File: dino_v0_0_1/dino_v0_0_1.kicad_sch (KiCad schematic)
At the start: 17 parts, among them SW1 SW_DIP_x07, U1 74LS590, U2 74LS590, U3 NE555P

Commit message: Schematic WIP
Updated Document as well.
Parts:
- added B1: Reset, symbol Switch:SW_Push
- added C1: 1µF, symbol Device:C_Small
- added C2: 0.1µF, symbol Device:C_Small
- added R1: R, symbol Device:R
- added R1: 1kΩ, symbol Device:R
- added R2: 100kΩ, symbol Device:R
- B2: renamed from Write; value Button 1 -> Write
- B3: renamed from Increment; value Button 2 -> Increment Addr
- MCM60256AP: value ~ -> SRAM
- SPDT: renamed from RUN/LOAD; value Mode Switch -> LOAD/RUN
- renumbered 74LS1 to 74LS645, U2 to HighCounter, U1 to LowCounter, U3 to SystemTimer
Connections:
- net ASTABLE_MODE: now reaches SystemTimer.2 (TR)
- net ASTABLE_MODE: now also SystemTimer.6 (THR), C1.1, R2.2
- net Timer output: now reaches SystemTimer.3 (Q)
- net Timer output: now also LowCounter.11 (CPC)
- net at SystemTimer.5 (CV): now also C2.1
- net at SystemTimer.7 (DIS): now also R1.2, R2.1
- net RESET: now reaches LowCounter.10 (~{MRC})
- net RESET: now also HighCounter.10 (~{MRC}), B1.1
- net Ripple Cascade: now reaches LowCounter.9 (~{RCO})
- net Ripple Cascade: now also HighCounter.11 (CPC)
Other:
- moved on the sheet: 74LS645, D1, D2, D3, D4, D5, D6, D7, D8, HighCounter, LowCounter, MCM60256AP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

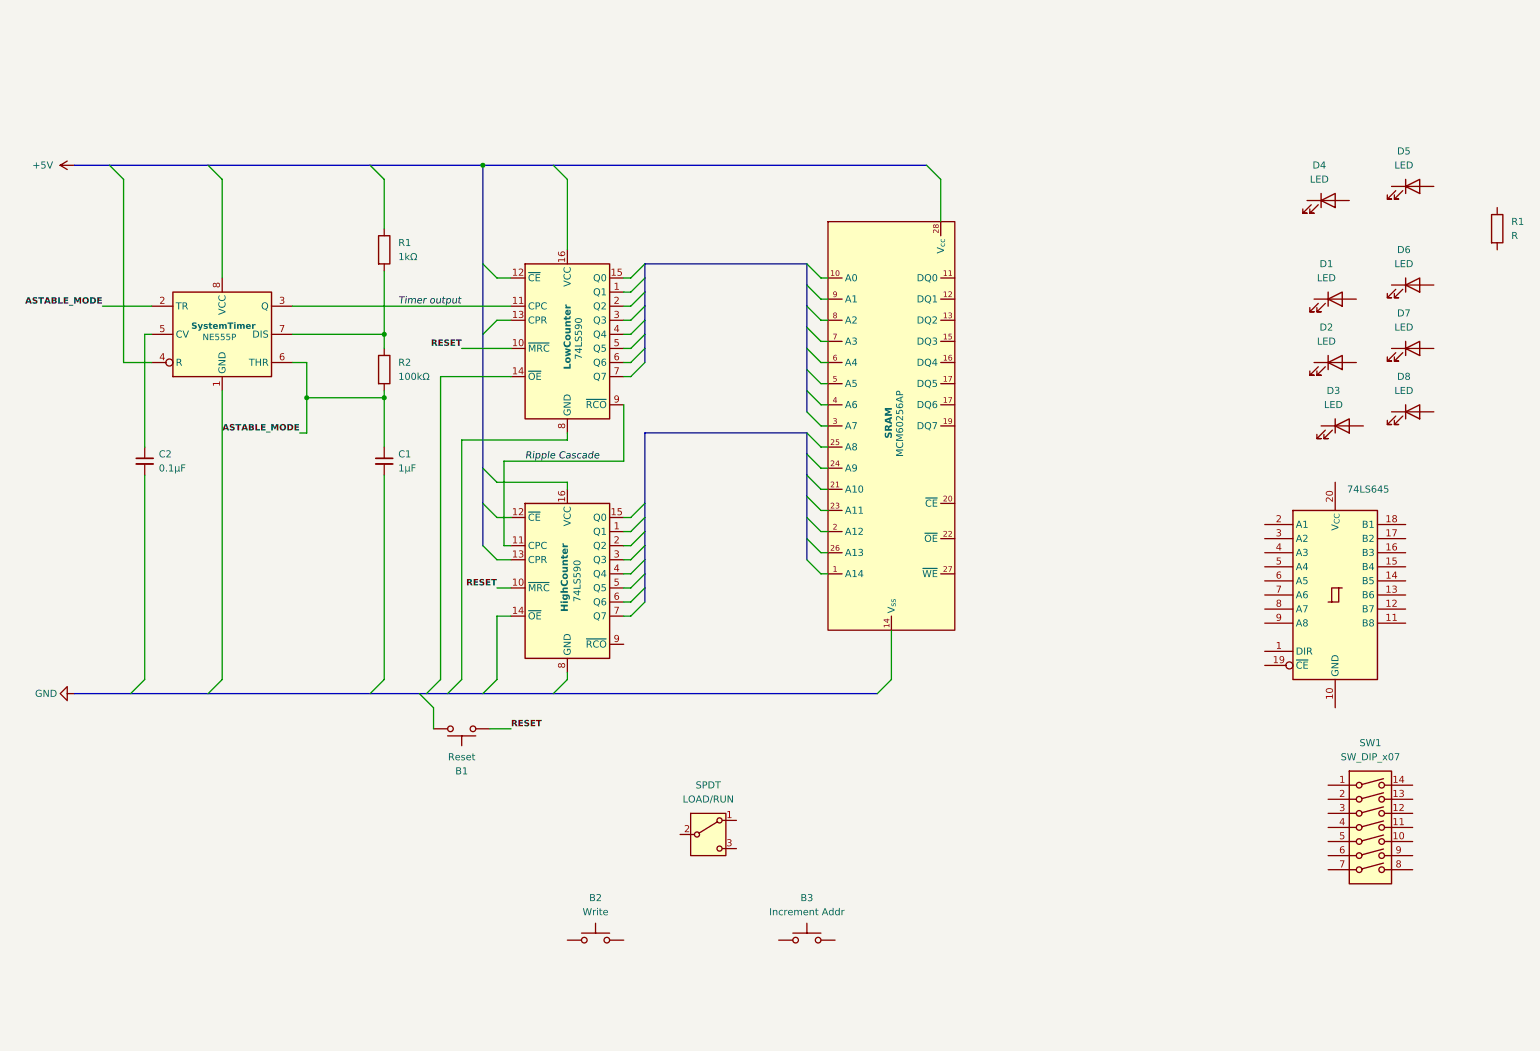
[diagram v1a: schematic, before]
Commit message: Updated D.I.N.O v0.0.2 Schematic
Discrete Integrated NISC Operator
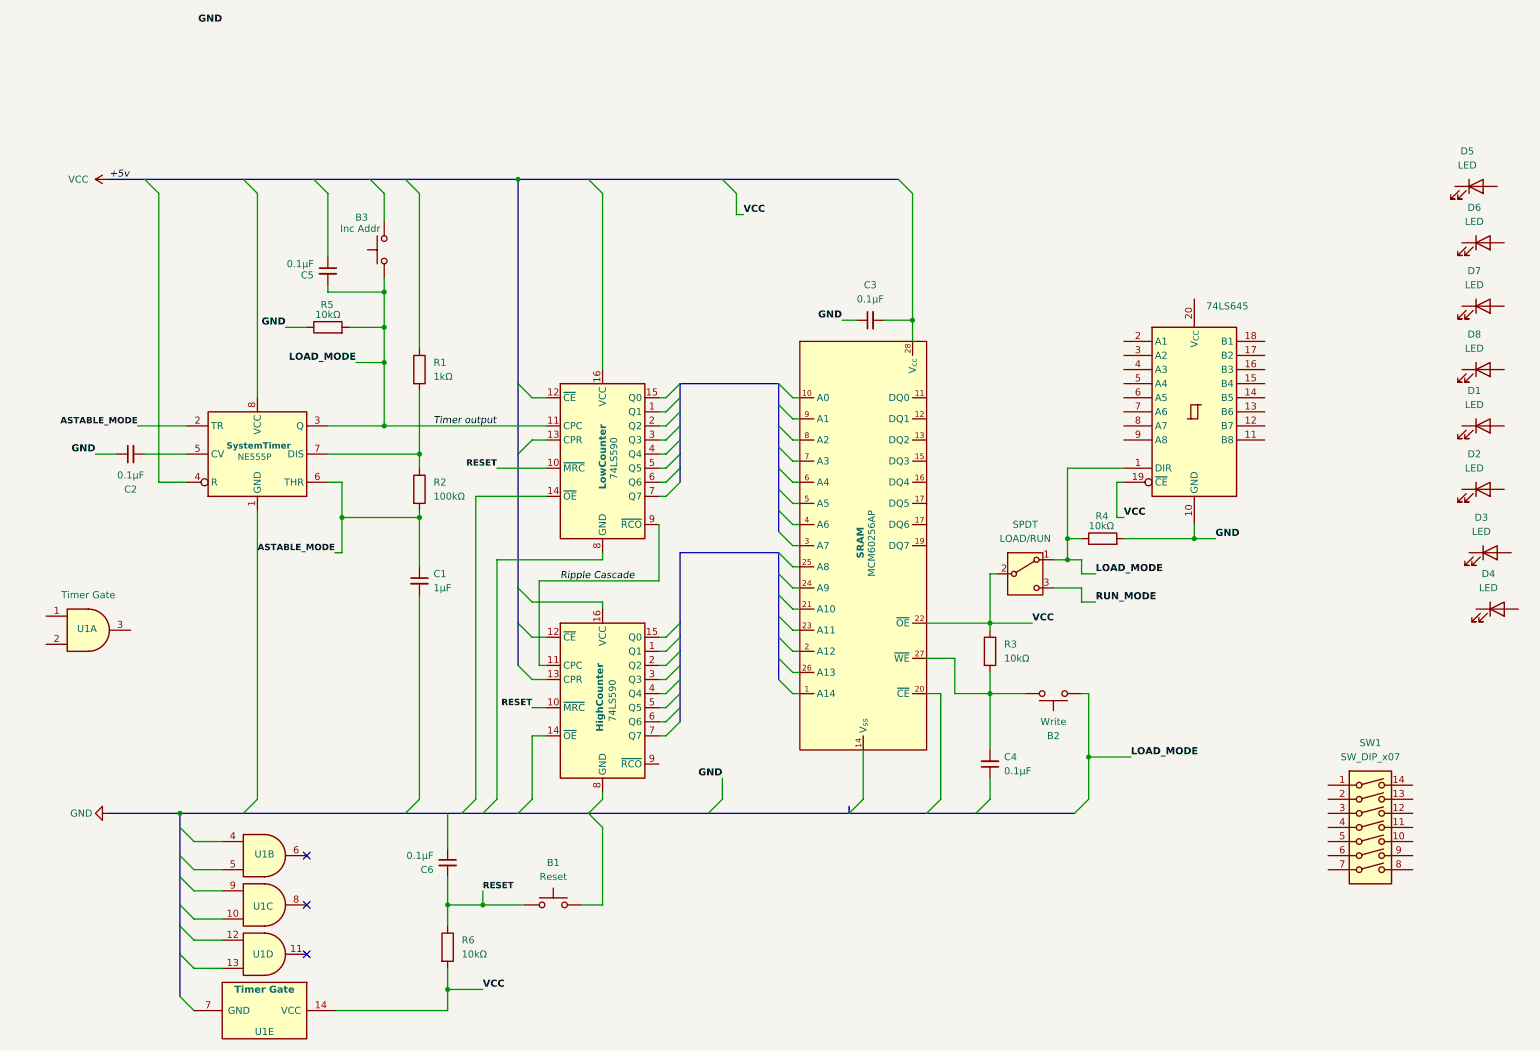
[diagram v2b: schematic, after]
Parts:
- removed R1: R, symbol Device:R
- added C3, C4, C5, C6: 0.1µF, symbol Device:C_Small
- added R3, R4, R5, R6: 10kΩ, symbol Device:R
- added U1: Timer Gate, symbol 74xx:74LS08
- B3: value Increment Addr -> Inc Addr
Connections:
- net Timer output is gone; now on net LOAD_MODE: LowCounter.11 (CPC), SystemTimer.3 (Q)
- net GND: now also 74LS645.10 (GND), C2.1, C3.1, R4.2, R5.1
- net RESET: now also C6.2, R6.1
- net at SystemTimer.5 (CV): now also C2.2; no longer C2.1
- net LOAD_MODE: now reaches 74LS645.1 (DIR)
- net LOAD_MODE: now also B2.1, B3.1, SPDT.1 (A), C5.2, R4.1, R5.2
- net VCC: now reaches 74LS645.19 (~{CE})
- net VCC: now also MCM60256AP.22 (~{OE}), SPDT.2 (B), R3.1, R6.2, U1.14 (VCC)
- net RUN_MODE: now reaches SPDT.3 (C)
- net at B2.2: now also MCM60256AP.27 (~{WE}), C4.2, R3.2
- net at MCM60256AP.28 (V_{cc}): now also C3.2
- no-connect marks 0 -> 3
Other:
- company: (none) -> Grey Giant Technologies, LLC
- title: Dino v0.0.1 -> D.I.N.O
- moved on the sheet: 74LS645, B1, B2, B3, C1, C2, D1, D2, D3, D4, D5, D6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

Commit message: Adds initial version of Dino PDF
Introduces version 0.0.1 of the Dino schematic.
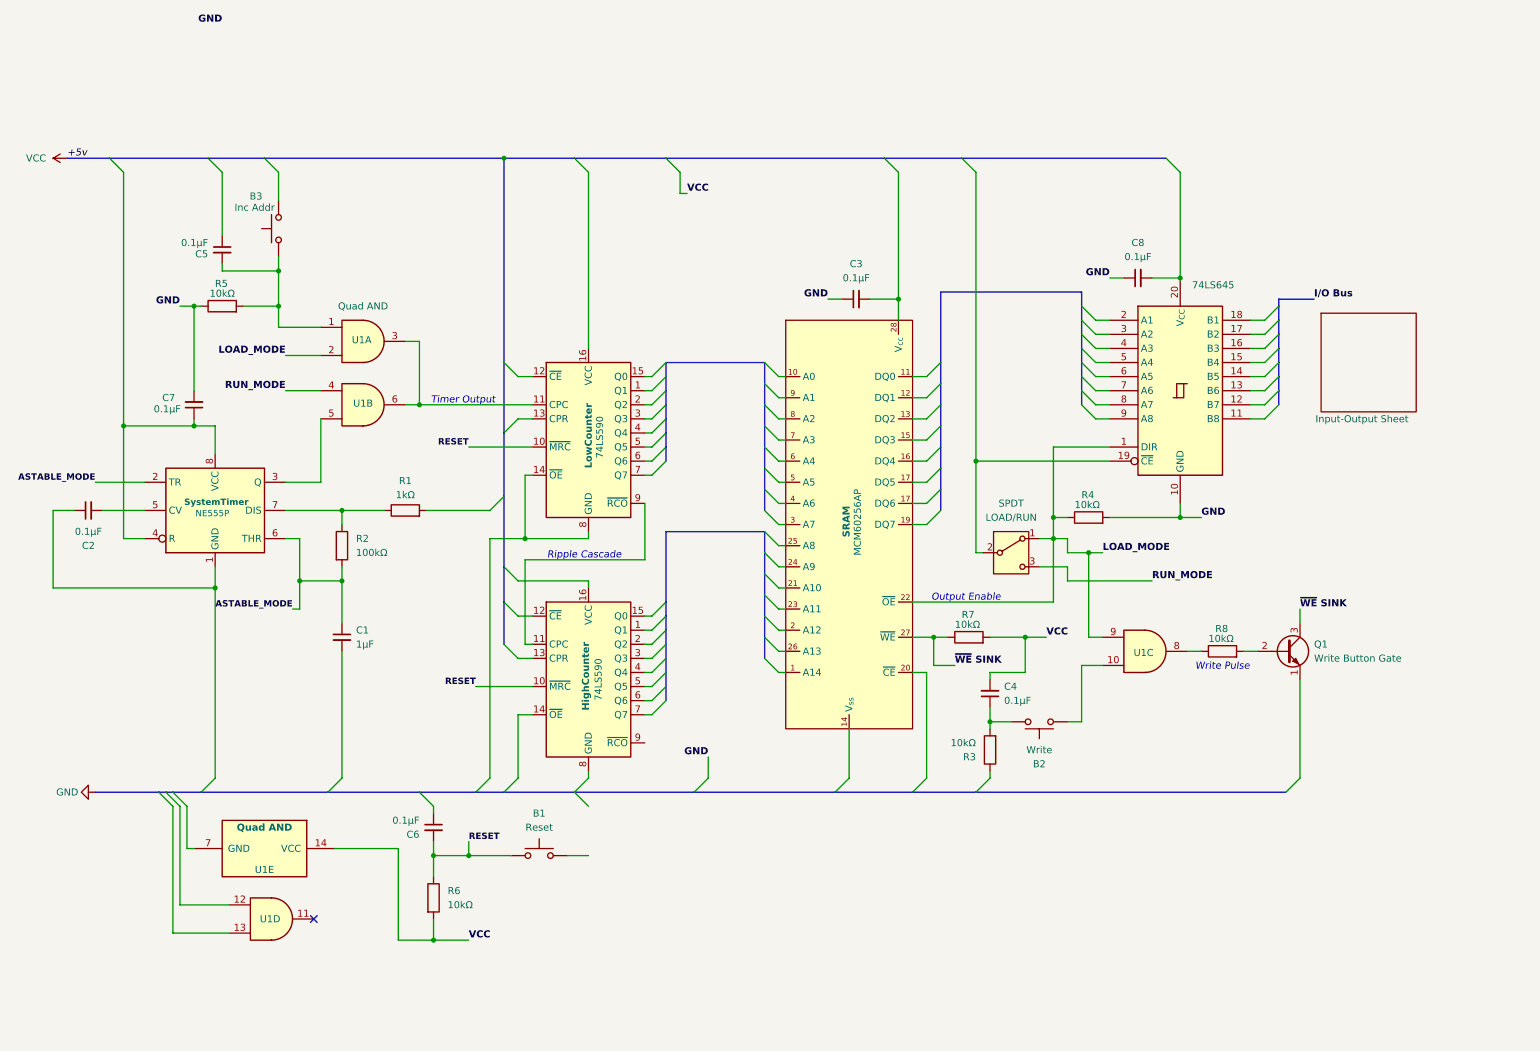
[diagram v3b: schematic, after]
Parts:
- removed D1, D2, D3, D4, D5, D6, D7, D8: LED, symbol Device:LED
- removed SW1: SW_DIP_x07, symbol Switch:SW_DIP_x07
- added C7, C8: 0.1µF, symbol Device:C_Small
- added Q1: Write Button Gate, Package_TO_SOT_THT:TO-92_Inline, symbol Transistor_BJT:2N3904
- added R7, R8: 10kΩ, symbol Device:R
- U1: value Timer Gate -> Quad AND
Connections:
- net GND: now also C7.2, C8.1; no longer C2.1
- net LOAD_MODE: now also MCM60256AP.22 (~{OE}), U1.2, U1.9; no longer B2.1, B3.1, C5.2, LowCounter.11 (CPC), R5.2, SystemTimer.3 (Q)
- net RUN_MODE: now also U1.4
- net VCC: now also C4.2, R7.2; no longer 74LS645.19 (~{CE}), MCM60256AP.22 (~{OE}), R3.1, SPDT.2 (B)
- net at C4.1: now also B2.2, R3.2
- net at SystemTimer.1 (GND): now also C2.1
- net at SystemTimer.4 (R): now also SystemTimer.8 (VCC), C7.1
- net at R2.1, SystemTimer.7 (DIS): now also R1.1; no longer R1.2
- net at U1.5: now also SystemTimer.3 (Q)
- net at U1.6: now also LowCounter.11 (CPC), U1.3
- net at 74LS645.20 (V_{CC}): now also C8.2
- net at LowCounter.14 (~{OE}): now also LowCounter.8 (GND)
- net at U1.10: now also B2.1
- net at U1.8: now also R8.1
- net at U1.1: now also B3.1, C5.2, R5.2
- net Ripple Cascade: no longer names the net of HighCounter.11 (CPC), LowCounter.9 (~{RCO})
- new net: Q1.2 (B), R8.2
- new net: 74LS645.19 (~{CE}), SPDT.2 (B)
- new net ~{WE} SINK: MCM60256AP.27 (~{WE}), Q1.3 (C), R7.1
- no-connect marks 3 -> 1
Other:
- added sheet Input-Output Sheet (input_output.kicad_sch)
- note added: "Output Enable"
- note added: "Ripple Cascade"
- note added: "Timer Output"
- note added: "Write Pulse"
- company: Grey Giant Technologies, LLC -> (none)
- title: D.I.N.O -> Dino v0.0.1
- moved on the sheet: 74LS645, B1, B2, B3, C1, C2, C3, C4, C5, C6, HighCounter, LowCounter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
